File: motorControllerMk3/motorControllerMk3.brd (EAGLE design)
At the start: 54.6 x 49.2 mm, 43 parts, among them J1 AVR_SPI_PRG_6NS, Y1 16MHz

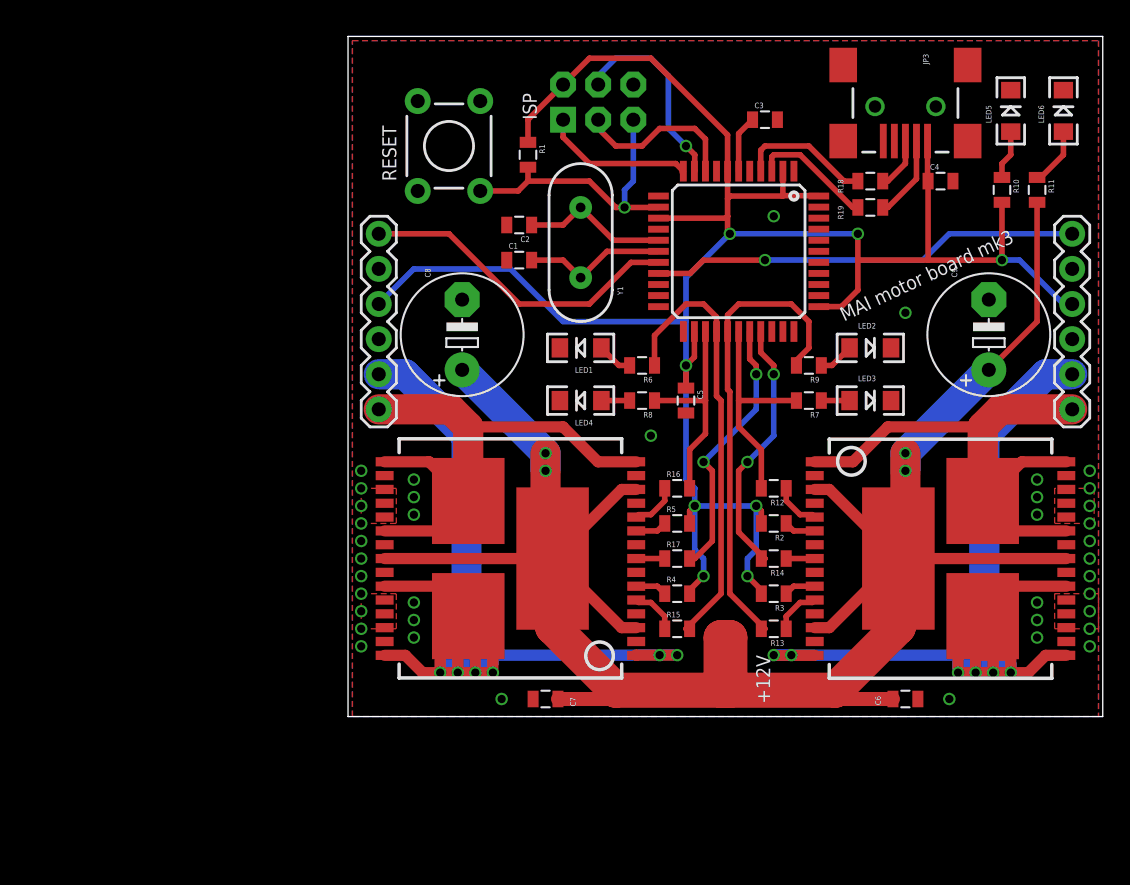
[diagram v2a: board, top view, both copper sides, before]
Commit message: optimizing ground plane and silk screen
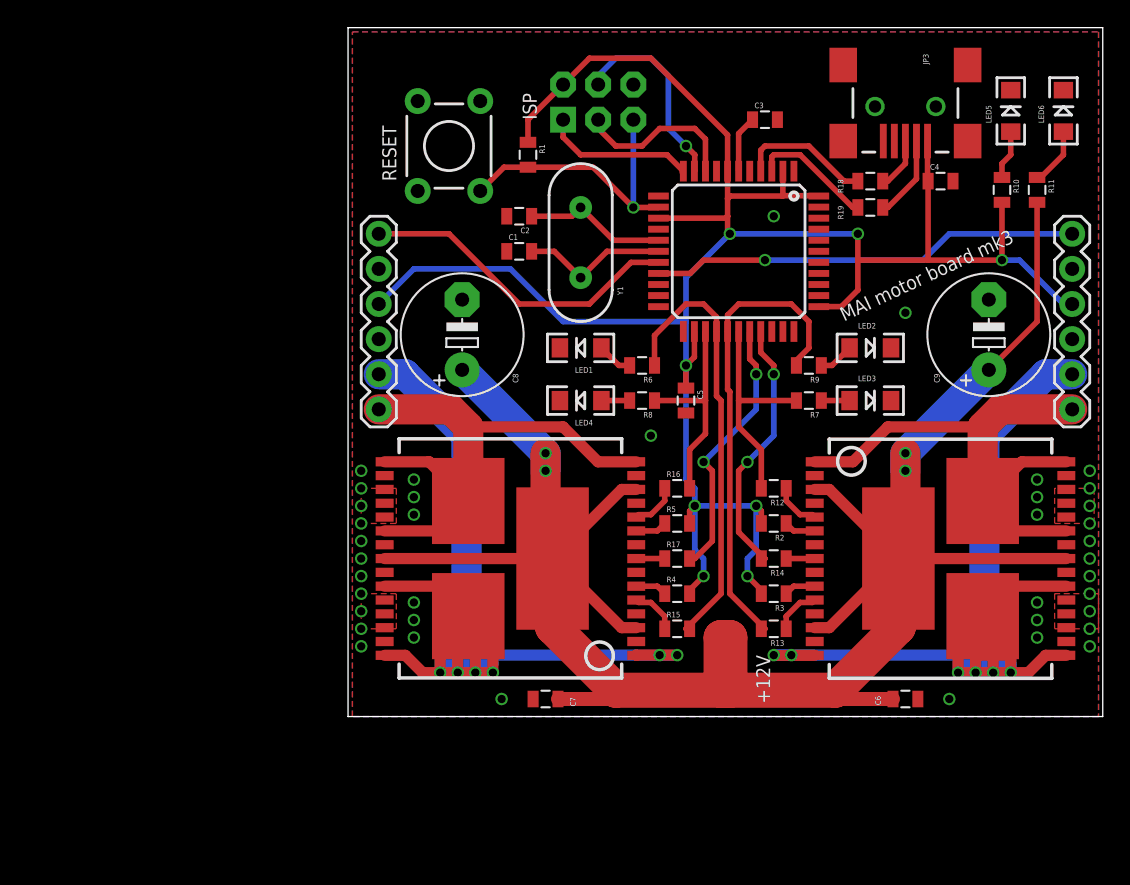
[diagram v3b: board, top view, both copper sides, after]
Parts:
- moved C1 0.63 mm to (35.6, 43.8)
- moved C2 0.63 mm to (35.6, 46.4)
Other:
- board size 54.6 x 49.2 mm -> 54.6 x 49.8 mm

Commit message: added mounting holes
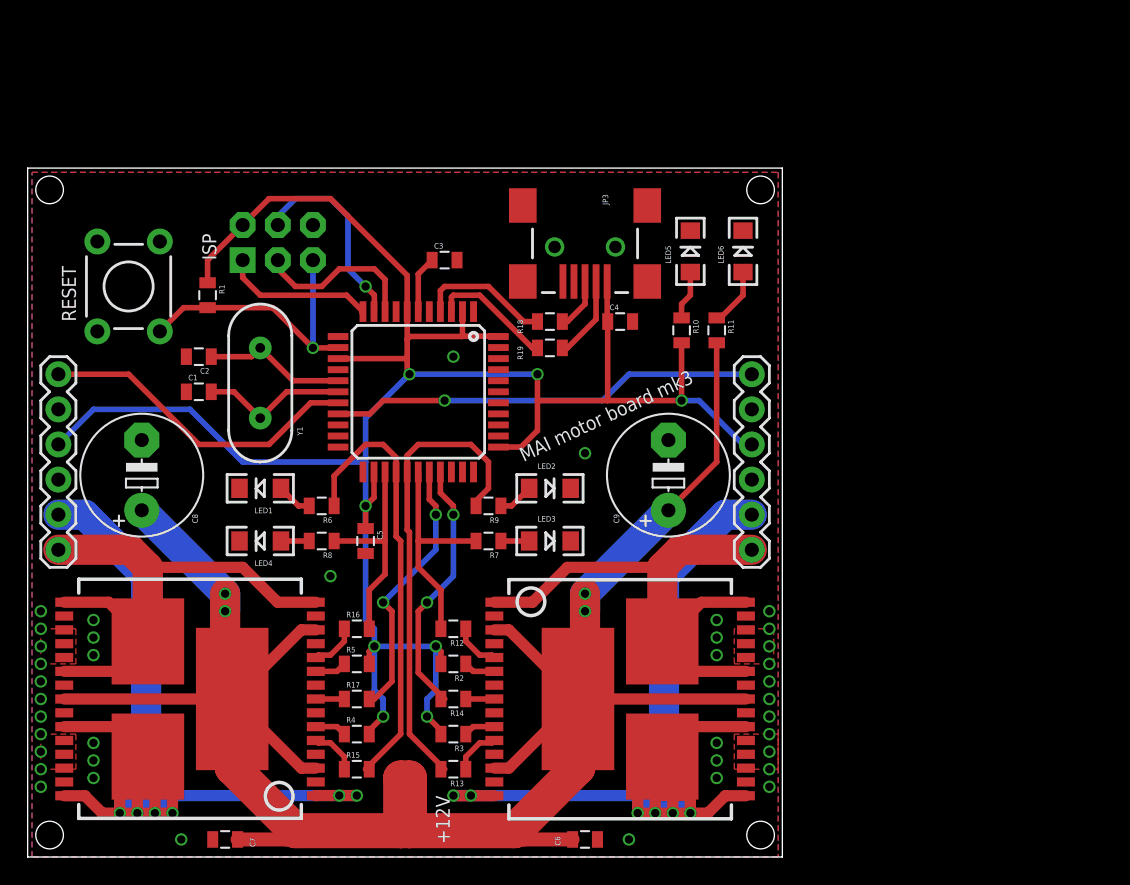
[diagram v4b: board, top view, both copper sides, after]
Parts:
- moved C4 25.3 mm to (42.9, 38.7)
- moved LED6 25.3 mm to (51.8, 43.8)
- moved R11 25.3 mm to (49.8, 38.1)
- moved U$3 25.3 mm to (42.9, 11.4)
- moved C3 25.3 mm to (30.2, 43.2)
- moved LED3 25.3 mm to (37.8, 22.9)
- moved LED4 25.3 mm to (16.8, 22.9)
- moved LED5 25.3 mm to (47.9, 43.8)
- moved R13 25.3 mm to (30.8, 6.35)
- moved R15 25.3 mm to (23.8, 6.35)
- moved R18 25.3 mm to (37.8, 38.7)
- moved R19 25.3 mm to (37.8, 36.8)
- moved R6 25.3 mm to (21.3, 25.4)
- moved R7 25.3 mm to (33.3, 22.9)
- moved R8 25.3 mm to (21.3, 22.9)
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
